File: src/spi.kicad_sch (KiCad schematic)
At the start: 0 parts

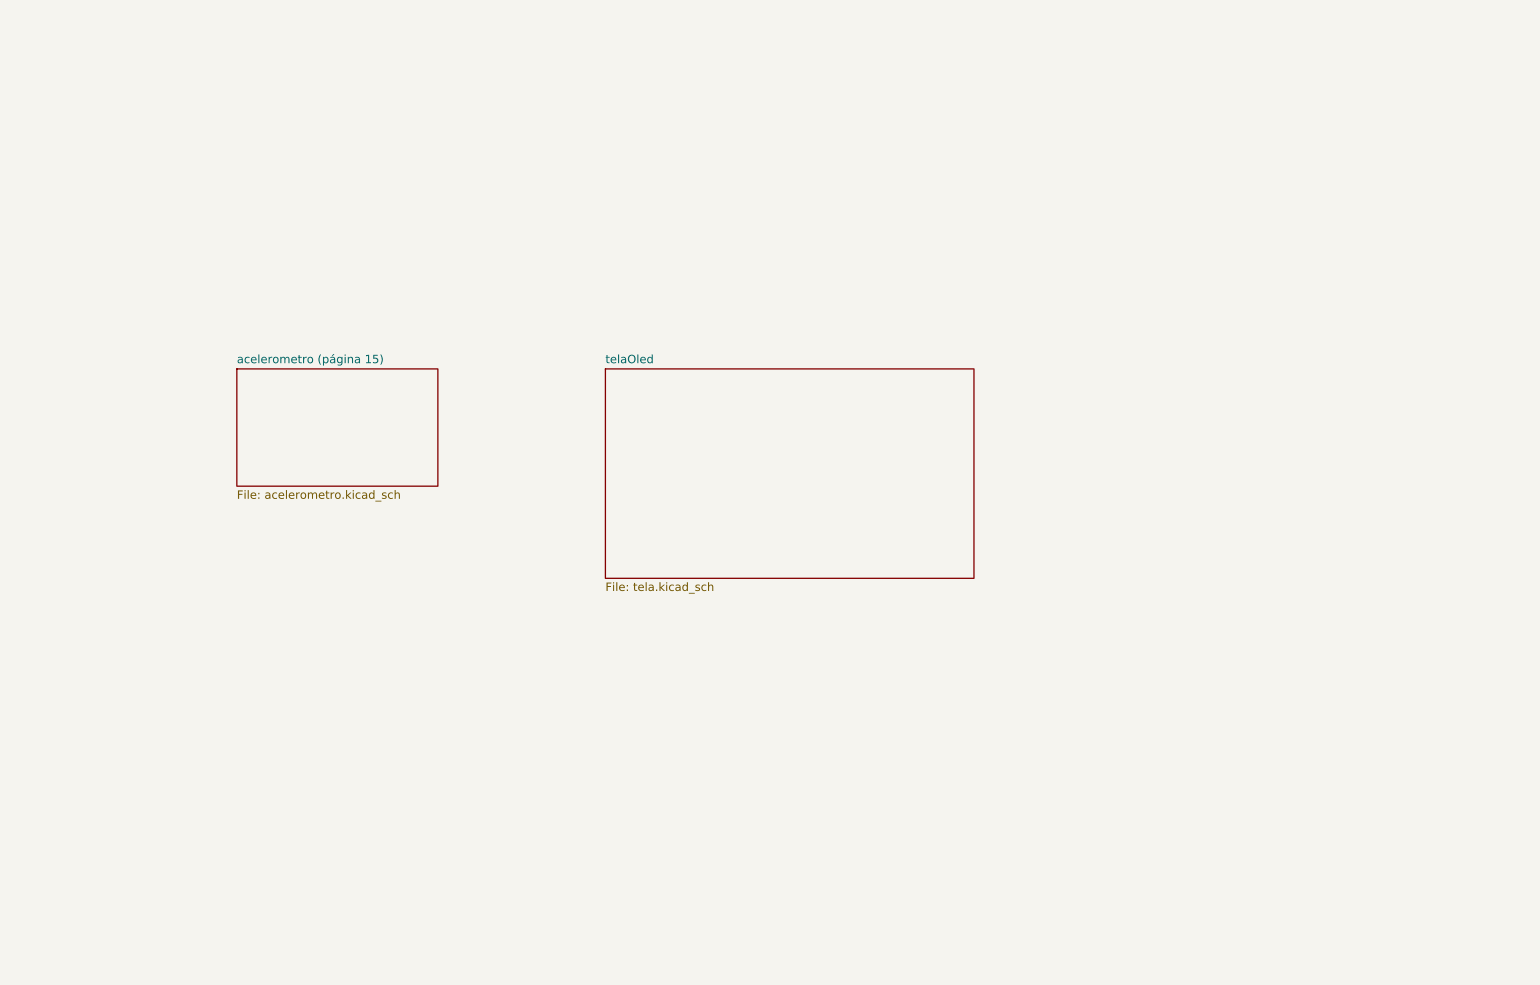
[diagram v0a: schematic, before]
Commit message: fix: Consertando paginação e refact da Tela_OLED
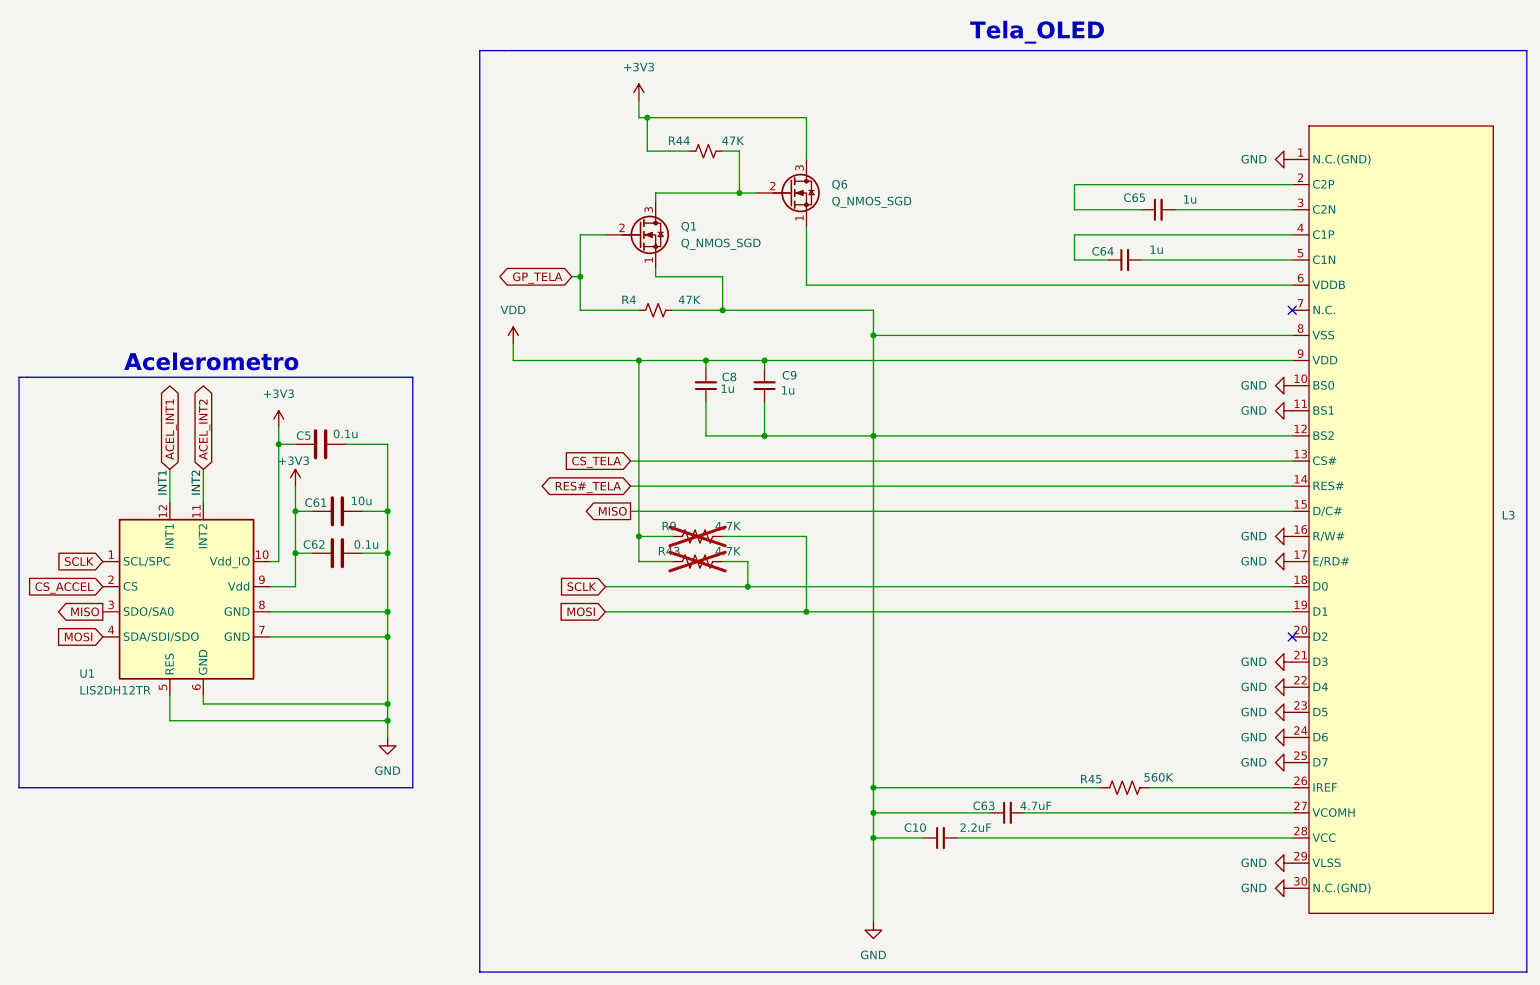
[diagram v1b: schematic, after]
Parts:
- added C10: 2.2uF, Capacitor_SMD:C_0402_1005Metric, symbol Device:C_Small
- added C5, C62: 0.1u, symbol Device:C
- added C61: 10u, symbol Device:C
- added C63: 4.7uF, Capacitor_SMD:C_0402_1005Metric, symbol Device:C_Small
- added C64, C65, C8, C9: 1u, Capacitor_SMD:C_0402_1005Metric, symbol Device:C_Small
- added L3: ~, symbol componentes_personalizados:Led_1.3
- added Q1, Q6: Q_NMOS_SGD, symbol Transistor_FET:Q_NMOS_SGD
- added R4, R44: 47K, Resistor_SMD:R_0402_1005Metric, symbol Device:R_Small_US
- added R43, R9: 4.7K, Resistor_SMD:R_0402_1005Metric, symbol Device:R_US
- added R45: 560K, Resistor_SMD:R_0402_1005Metric, symbol Device:R_US
- added U1: LIS2DH12TR, Package_LGA:LGA-14_2x2mm_P0.35mm_LayoutBorder3x4y, symbol Sensor_Motion:LIS2DH
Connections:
- new net: C65.1, L3.2 (C2P)
- new net: C65.2, L3.3 (C2N)
- new net: C63.2, L3.27 (VCOMH)
- new net: L3.6 (VDDB), Q6.1 (S)
- new net: Q1.3 (D), Q6.2 (G), R44.2
- new net: C64.1, L3.4 (C1P)
- new net: C64.2, L3.5 (C1N)
- new net: C10.2, L3.28 (VCC)
- new net: L3.26 (IREF), R45.2
- new net +3V3: C5.2, C61.2, C62.2, Q6.3 (D), R44.1, U1.10 (Vdd_IO), U1.9 (Vdd)
- new net ACEL_INT1: U1.12 (GND)
- new net ACEL_INT2: U1.11 (INT2)
- new net CS_ACCEL: U1.2 (CS)
- new net CS_TELA: L3.13 (CS#)
- new net GND: C10.1, C5.1, C61.1, C62.1, C63.1, C8.1, C9.1, L3.1 (N.C.(GND)), L3.10 (BS0), L3.11 (BS1), L3.12 (BS2), L3.16 (R/W#), L3.17 (E/RD#), L3.21 (D3), L3.22 (D4), L3.23 (D5), L3.24 (D6), L3.25 (D7), L3.29 (VLSS), L3.30 (N.C.(GND)), L3.8 (VSS), Q1.1 (S), R4.2, R45.1, U1.10 (Vdd_IO), U1.11 (INT2), U1.12 (GND), U1.13 (GND), U1.14 (GND), U1.5 (RES), U1.6 (GND), U1.7 (GND), U1.8 (GND)
- new net GP_TELA: Q1.2 (G), R4.1
- new net MISO: L3.15 (D/C#), U1.3 (SDO/SA0)
- new net MOSI: L3.19 (D1), R9.2, U1.4 (SDA/SDI/SDO)
- new net RES#_TELA: L3.14 (RES#)
- new net SCLK: L3.18 (D0), R43.2, U1.1 (SCL/SPC)
- new net VDD: C8.2, C9.2, L3.9 (VDD), R43.1, R9.1
- no-connect marks 0 -> 2
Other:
- removed sheet acelerometro (página 15)
- removed sheet telaOled
- note added: "Acelerometro"
- note added: "Tela_OLED"

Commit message: adicionado footprints, falta microfone e display somente
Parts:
- C5, C61, C62: footprint (none) -> Capacitor_SMD:C_0402_1005Metric
- Q1, Q6: footprint (none) -> componentes_personalizados:mosfet-DMN2600UFB-7
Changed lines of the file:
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@@
 			)
 		)
-		(property "Footprint" ""
+		(property "Footprint" "componentes_personalizados:mosfet-DMN2600UFB-7"
 			(at 158.75 43.18 0)
 			(effects
@@
 			)
 		)
-		(property "Footprint" ""
+		(property "Footprint" "Capacitor_SMD:C_0402_1005Metric"
 			(at 78.74 84.7852 0)
 			(effects
@@
 			)
 		)
-		(property "Footprint" ""
+		(property "Footprint" "componentes_personalizados:mosfet-DMN2600UFB-7"
 			(at 135.89 49.53 0)
 			(effects
@@
 			)
 		)
-		(property "Footprint" ""
+		(property "Footprint" "Capacitor_SMD:C_0402_1005Metric"
 			(at 81.28 101.2952 0)
 			(effects
@@
 			)
 		)
-		(property "Footprint" ""
+		(property "Footprint" "Capacitor_SMD:C_0402_1005Metric"
 			(at 81.28 94.9452 0)
 			(effects

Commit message: Subconjuntos organizados na PCI
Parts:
- L3: footprint (none) -> Display:OLED-128O064D
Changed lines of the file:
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@@
 			)
 		)
-		(property "Footprint" ""
+		(property "Footprint" "Display:OLED-128O064D"
 			(at 231.14 33.02 0)
 			(effects
